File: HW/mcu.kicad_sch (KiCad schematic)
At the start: 11 parts, among them J1 SWD, J2 UART, J3 USB C, SW1 Reset, U1 STM32WB55CGUx, U2 USBLC6-2SC6, Y1 32MHz

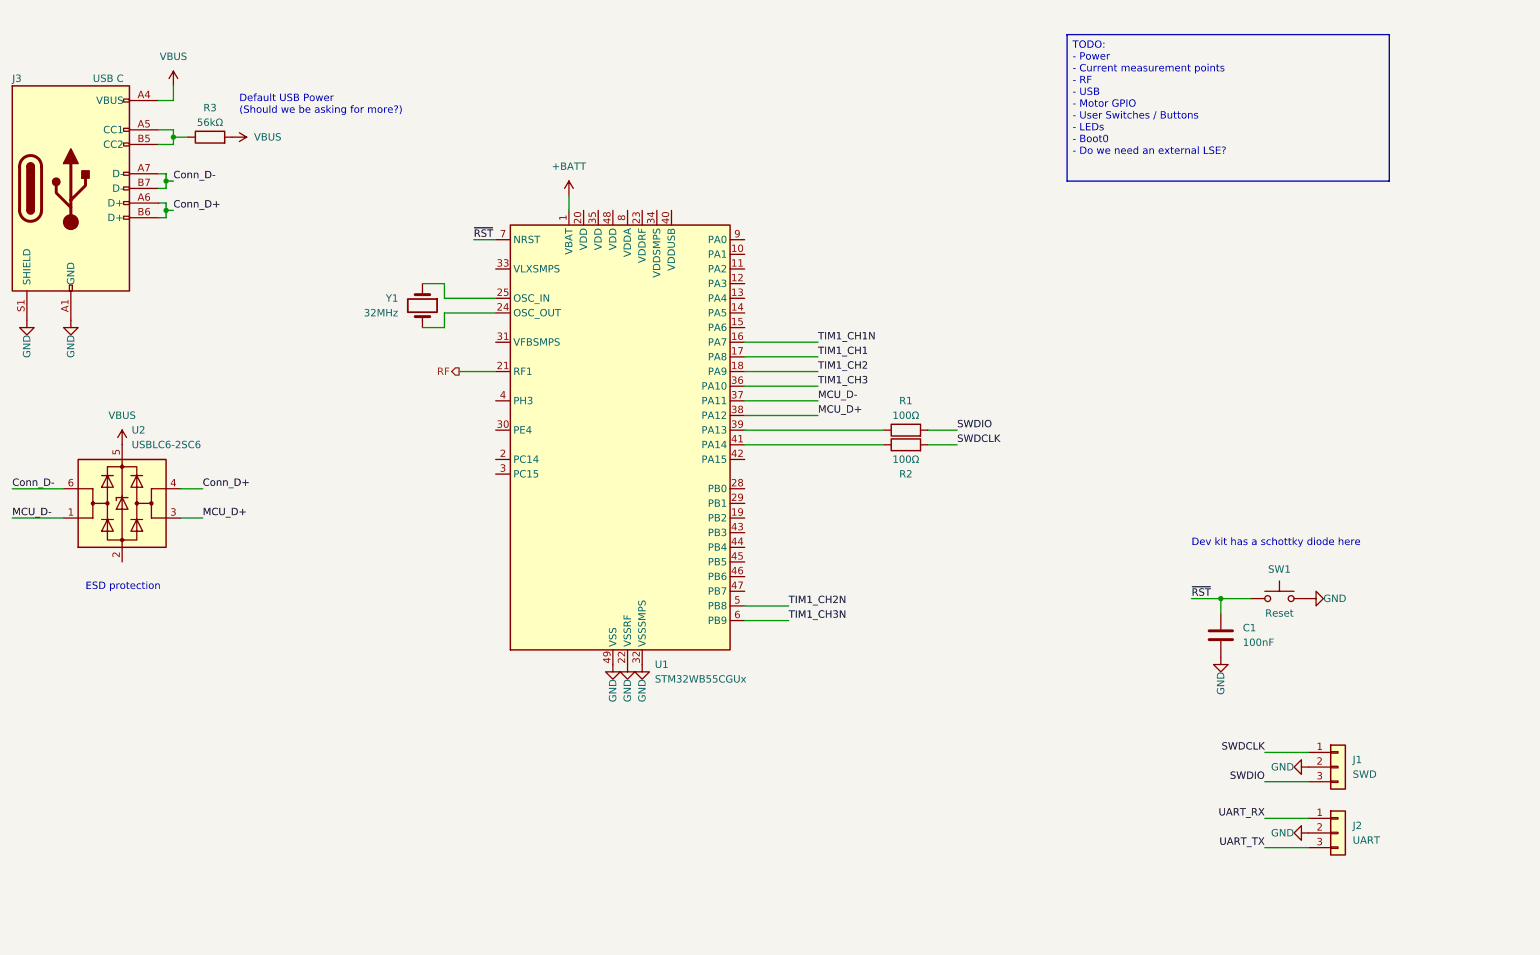
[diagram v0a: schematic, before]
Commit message: Almost first schematic draft (missing resistor values for STDRIVE current sensing and leds)
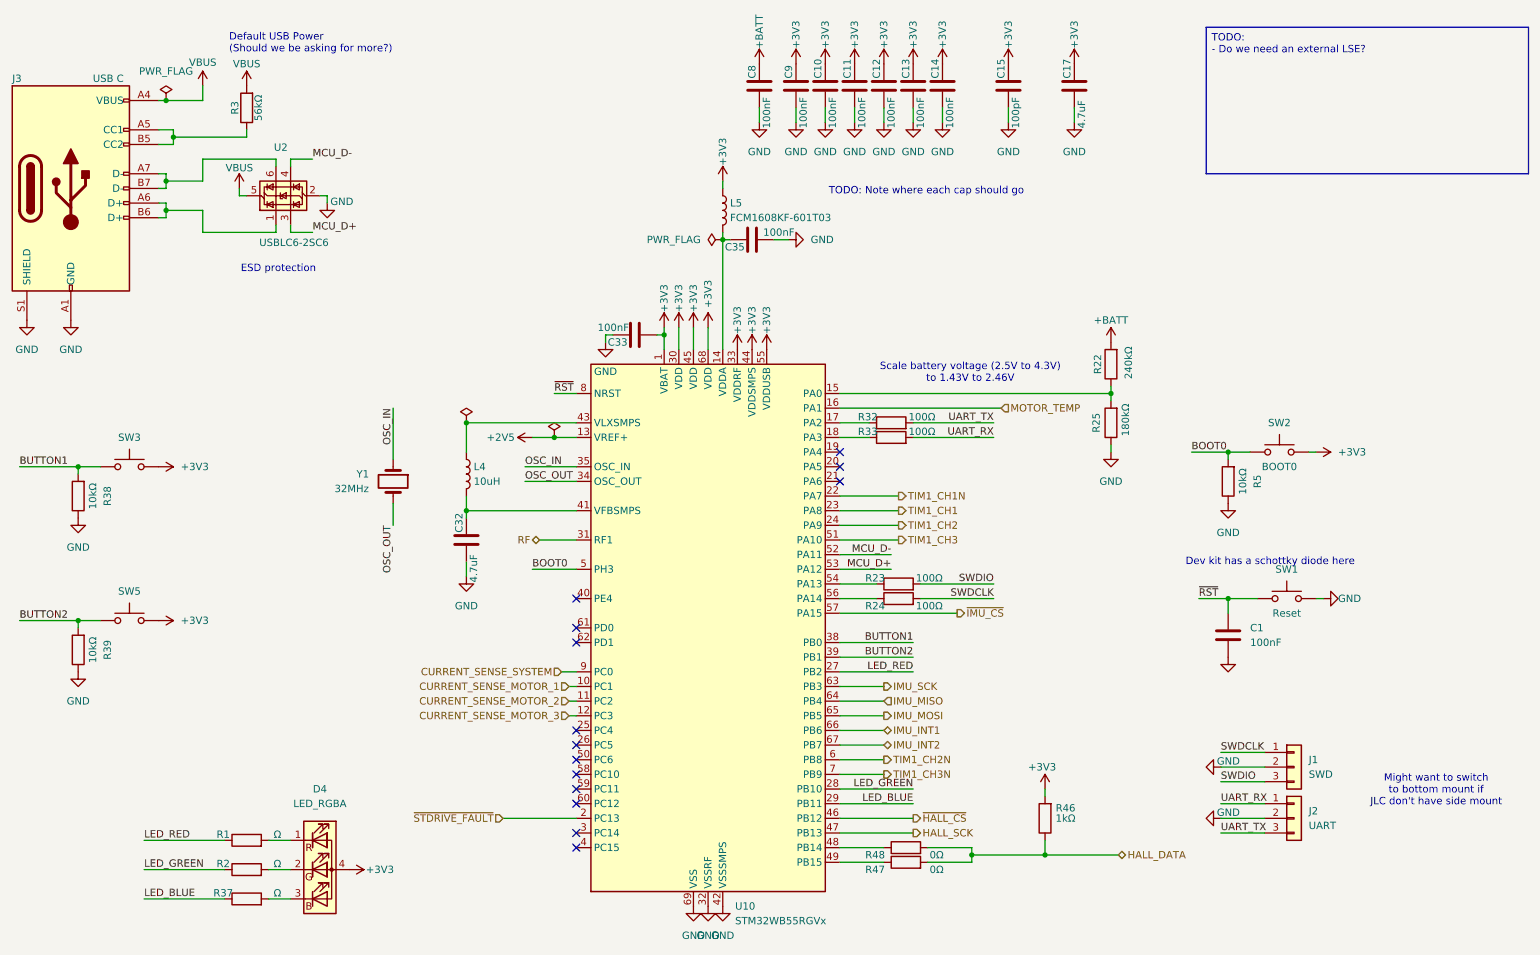
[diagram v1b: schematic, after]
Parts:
- removed U1: STM32WB55CGUx, Package_DFN_QFN:QFN-48-1EP_7x7mm_P0.5mm_EP5.6x5.6mm, symbol MCU_ST_STM32WB:STM32WB55CGUx
- added C10, C11, C12, C13, C14, C33, C35, C8, C9: 100nF, Capacitor_SMD:C_0402_1005Metric, symbol Device:C
- added C15: 100pF, Capacitor_SMD:C_0402_1005Metric, symbol Device:C
- added C17, C32: 4.7uF, Capacitor_SMD:C_0402_1005Metric, symbol Device:C
- added D4: LED_RGBA, symbol Device:LED_RGBA
- added L4: 10uH, Inductor_SMD:L_0603_1608Metric, symbol Device:L
- added L5: FCM1608KF-601T03, Inductor_SMD:L_0603_1608Metric, symbol Device:L
- added R22: 240kΩ, Resistor_SMD:R_0402_1005Metric, symbol Device:R
- added R23, R24, R32, R33: 100Ω, Resistor_SMD:R_0402_1005Metric, symbol Device:R
- added R25: 180kΩ, Resistor_SMD:R_0402_1005Metric, symbol Device:R
- added R37: Ω, Resistor_SMD:R_0402_1005Metric, symbol Device:R
- added R38, R39, R5: 10kΩ, Resistor_SMD:R_0402_1005Metric, symbol Device:R
- added R46: 1kΩ, Resistor_SMD:R_0402_1005Metric, symbol Device:R
- added R47, R48: 0Ω, Resistor_SMD:R_0402_1005Metric, symbol Device:R
- added SW2, SW3, SW5: BOOT0, symbol Switch:SW_Push
- added U10: STM32WB55RGVx, Package_DFN_QFN:QFN-68-1EP_8x8mm_P0.4mm_EP6.4x6.4mm, symbol MCU_ST_STM32WB:STM32WB55RGVx
- C1: footprint (none) -> Capacitor_SMD:C_0402_1005Metric
- R1, R2: value 100Ω -> Ω; footprint (none) -> Resistor_SMD:R_0402_1005Metric
- R3: footprint (none) -> Resistor_SMD:R_0402_1005Metric
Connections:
- net +BATT: now also C8.1, R22.2
- net GND: now also U2.2 (GND), C10.2, C11.2, C12.2, C13.2, C14.2, C15.2, C17.2, C32.2, C33.1, C35.2, C8.2, C9.2, R25.1, R38.1, R39.1, R5.1, U10.32 (VSSRF), U10.42 (VSSSMPS), U10.69 (VSS)
- net MCU_D+: now also U10.53 (PA12)
- net MCU_D-: now also U2.4 (I/O2), U10.52 (PA11); no longer U2.1 (I/O1)
- net RF: now also U10.31 (RF1)
- net SWDCLK: now also R24.2; no longer R2.2
- net SWDIO: now also R23.2; no longer R1.2
- net TIM1_CH1: now also U10.23 (PA8)
- net TIM1_CH1N: now also U10.22 (PA7)
- net TIM1_CH2: now also U10.24 (PA9)
- net TIM1_CH2N: now also U10.6 (PB8)
- net TIM1_CH3: now also U10.51 (PA10)
- net TIM1_CH3N: now also U10.7 (PB9)
- net UART_RX: now also R33.2
- net UART_TX: now also R32.2
- net ~{RST}: now also U10.8 (NRST)
- net LED_RED: now reaches R1.1
- net LED_RED: now also U10.27 (PB2)
- net OSC_OUT: now reaches Y1.2
- net OSC_OUT: now also U10.34 (OSC_OUT)
- net OSC_IN: now reaches Y1.1
- net OSC_IN: now also U10.35 (OSC_IN)
- net LED_GREEN: now reaches R2.1
- net LED_GREEN: now also U10.28 (PB10)
- net Conn_D+: no longer names the net of J3.A6 (D+), J3.B6 (D+)
- net Conn_D+: now also U2.1 (I/O1); no longer U2.4 (I/O2)
- net Conn_D-: no longer names the net of J3.A7 (D-), J3.B7 (D-), U2.6 (I/O1)
- new net: D4.1 (RK), R1.2
- new net: R47.1, U10.49 (PB15)
- new net: R48.1, U10.48 (PB14)
- new net: D4.2 (GK), R2.2
- new net: C35.1, L5.2, U10.14 (VDDA)
- new net: R22.1, R25.2, U10.15 (PA0)
- new net: R32.1, U10.17 (PA2)
- new net: R33.1, U10.18 (PA3)
- new net: C32.1, L4.2, U10.41 (VFBSMPS)
- new net: L4.1, U10.43 (VLXSMPS)
- new net: R23.1, U10.54 (PA13)
- new net: R24.1, U10.56 (PA14)
- new net: D4.3 (BK), R37.2
- new net +2V5: U10.13 (VREF+)
- new net +3V3: C10.1, C11.1, C12.1, C13.1, C14.1, C15.1, C17.1, C33.2, C9.1, D4.4 (A), L5.1, R46.2, SW2.2, SW3.2, SW5.2, U10.1 (VBAT), U10.30 (VDD), U10.33 (VDDRF), U10.44 (VDDSMPS), U10.45 (VDD), U10.55 (VDDUSB), U10.68 (VDD)
- new net BOOT0: R5.2, SW2.1, U10.5 (PH3)
- new net BUTTON1: R38.2, SW3.1, U10.38 (PB0)
- new net BUTTON2: R39.2, SW5.1, U10.39 (PB1)
- new net CURRENT_SENSE_MOTOR_1: U10.10 (PC1)
- new net CURRENT_SENSE_MOTOR_2: U10.11 (PC2)
- new net CURRENT_SENSE_MOTOR_3: U10.12 (PC3)
- new net CURRENT_SENSE_SYSTEM: U10.9 (PC0)
- new net HALL_DATA: R46.1, R47.2, R48.2
- new net HALL_SCK: U10.47 (PB13)
- new net IMU_INT1: U10.66 (PB6)
- new net IMU_INT2: U10.67 (PB7)
- new net IMU_MISO: U10.64 (PB4)
- new net IMU_MOSI: U10.65 (PB5)
- new net IMU_SCK: U10.63 (PB3)
- new net LED_BLUE: R37.1, U10.29 (PB11)
- new net MOTOR_TEMP: U10.16 (PA1)
- new net ~{HALL_CS}: U10.46 (PB12)
- new net ~{IMU_CS}: U10.57 (PA15)
- new net ~{STDRIVE_FAULT}: U10.2 (PC13)
- no-connect marks 0 -> 14
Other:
- note added: "Might want to switch to bottom mount if JLC don't have side mount"
- note added: "Scale battery voltage (2.5V to 4.3V) to 1.43V to 2.46V"
- note added: "TODO: Note where each cap should go"
- moved on the sheet: C1, J1, J2, R3, SW1, Y1

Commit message: Added resistor values for LED and removed STDRIVE current sensing
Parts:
- removed D4: LED_RGBA, symbol Device:LED_RGBA
- added D4: LED_RGB, LED_SMD:LED_RGB_5050-6, symbol lib:LED_RGB
- R1: value Ω -> 330Ω
- R2: value Ω -> 180Ω
- R37: value Ω -> 47Ω
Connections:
- net +3V3: now also D4.1 (GA), D4.2 (RA), D4.3 (BA)
- net at R1.2: now also D4.6 (GK)
- net at R2.2: now also D4.5 (RK)
- net at R37.2: now also D4.4 (BK)
- net LED_BLUE renamed LED3
- net LED3: no longer U10.29 (PB11)
- net LED_GREEN renamed LED2
- net LED2: no longer U10.28 (PB10)
- net LED_RED renamed LED1
- net LED1: no longer U10.27 (PB2)
- new net LED_1: U10.27 (PB2)
- new net LED_2: U10.28 (PB10)
- new net LED_3: U10.29 (PB11)
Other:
- moved on the sheet: R1, R2, R37

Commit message: Fixed USB ESD protection
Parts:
- R46: now not fitted
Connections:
- net MCU_D+: now also U2.4 (I/O2); no longer U2.3 (I/O2)
- net MCU_D-: now also U2.6 (I/O1); no longer U2.4 (I/O2)
- net at J3.A6 (D+), J3.B6 (D+): now also U2.3 (I/O2); no longer U2.1 (I/O1)
- net at J3.A7 (D-), J3.B7 (D-): now also U2.1 (I/O1); no longer U2.6 (I/O1)
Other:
- note added: "This resistor value might be for signalling a USB A cable is connected"
- moved on the sheet: R3, U2

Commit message: Cleaned up and implemented some of Laimonas' feedback
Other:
- company: (none) -> Roberto Holmes
- title: (none) -> Capstan
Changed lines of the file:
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@@
 	(generator_version "9.0")
 	(paper "A4")
+	(title_block
+		(title "Capstan")
+		(date "2025-09-26")
+		(company "Roberto Holmes")
+	)
 	(text "TODO: Note where each cap should go"
 		(exclude_from_sim no)
@@
 		)
 	)
-	(text_box "TODO:\n - Do we need an external LSE?"
-		(exclude_from_sim no)
-		(at 224.79 15.24 0)
-		(size 55.88 25.4)
-		(margins 0.9525 0.9525 0.9525 0.9525)
-		(stroke
-			(width 0)
-			(type solid)
-		)
-		(fill
-			(type none)
-		)
-		(effects
-			(font
-				(size 1.27 1.27)
-			)
-			(justify left top)
-		)
-	)
